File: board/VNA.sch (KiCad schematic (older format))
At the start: 63 parts, among them J1 Conn_01x08, J10 Conn_01x01, J11 Conn_01x01, J12 Conn_01x01, J13 Conn_01x01, J14 Conn_01x01, J15 Conn_02x05_Odd_Even, J16 Conn_02x05_Odd_Even, J17 Conn_01x04, J18 Conn_01x01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

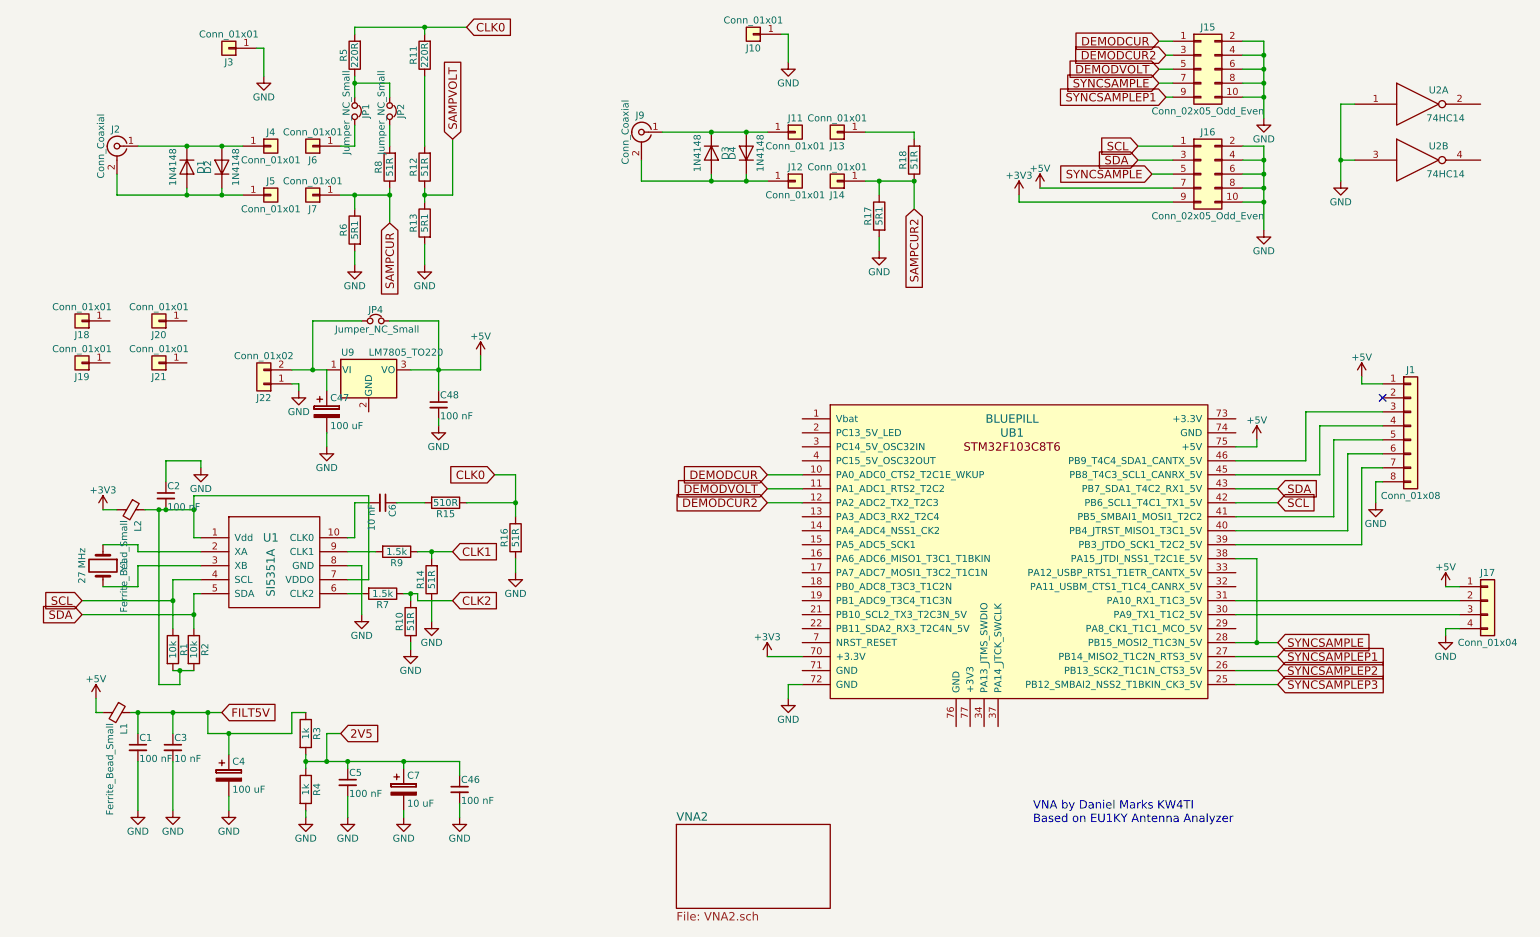
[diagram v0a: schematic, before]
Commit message: Removed useless parts of the board and make some corrections
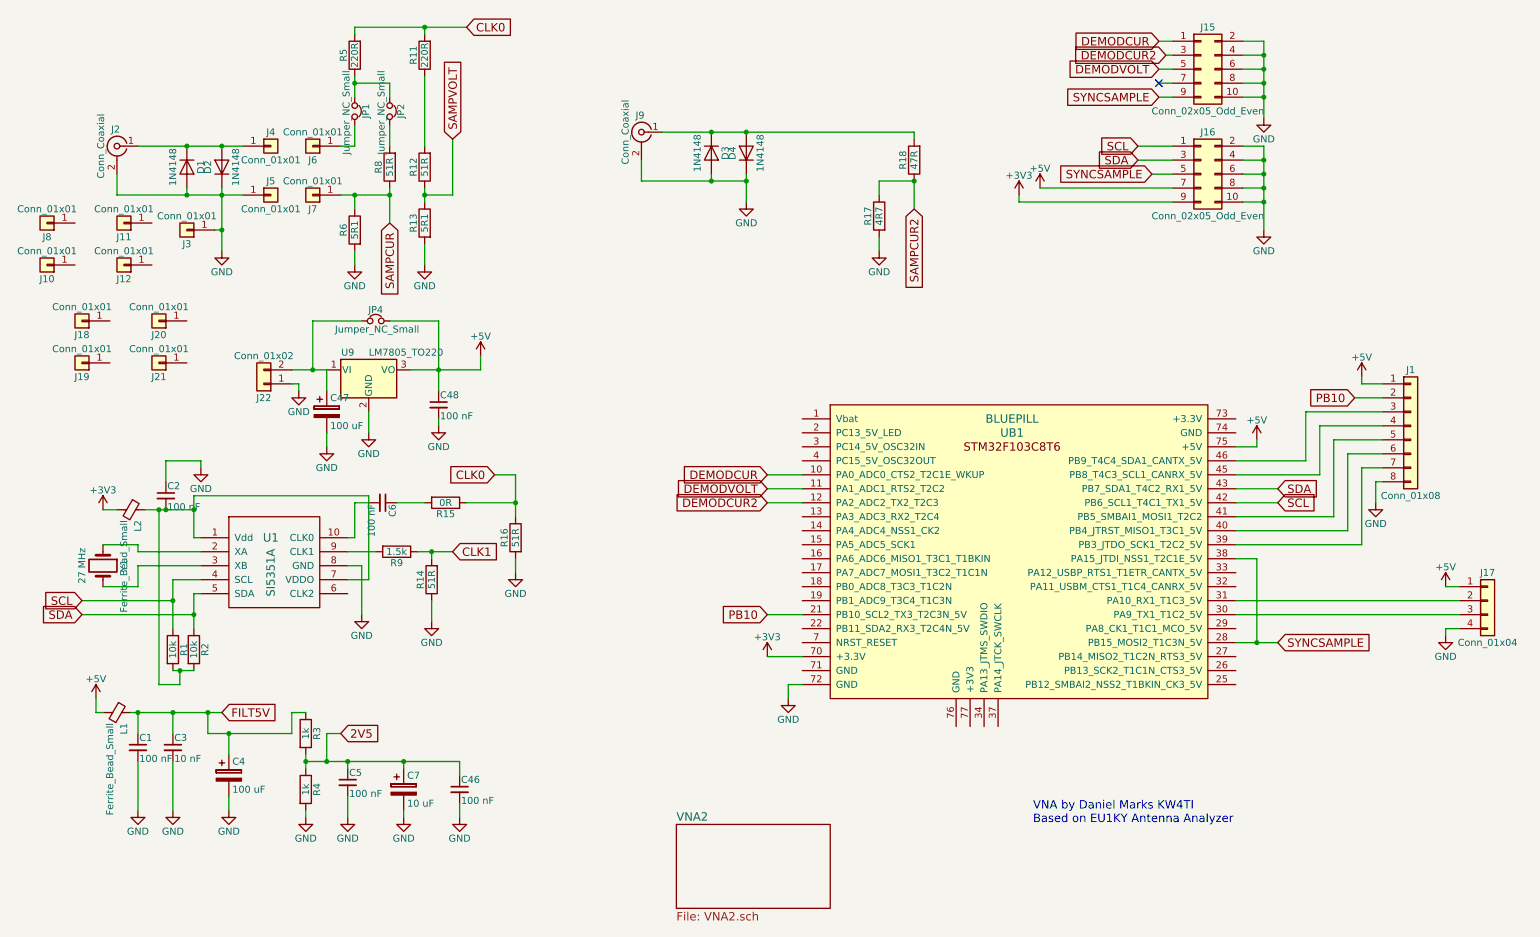
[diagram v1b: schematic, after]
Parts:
- removed J13, J14: Conn_01x01, Connectors:1pin, symbol Conn_01x01
- removed R10: 51R, Resistors_THT:R_Axial_DIN0207_L6.3mm_D2.5mm_P7.62mm_Horizontal, symbol R
- removed R7: 1.5k, Resistors_THT:R_Axial_DIN0207_L6.3mm_D2.5mm_P7.62mm_Horizontal, symbol R
- removed U2: 74HC14, Housings_DIP:DIP-14_W7.62mm_Socket, symbol 74HC14
- added J8: Conn_01x01, Connectors:1pin, symbol Conn_01x01
- C6: value 10 nF -> 100 nF
- R15: value 510R -> 0R
- R17: value 5R1 -> 4R7
- R18: value 51R -> 47R
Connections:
- net GND: now also D1.2 (A), D2.1 (K), D3.2 (A), D4.1 (K), J2.2 (Ext), J5.1 (Pin_1), J9.2 (Ext), U9.2 (GND); no longer J10.1 (Pin_1)
- net SYNCSAMPLE: now also J15.9 (Pin_9); no longer J15.7 (Pin_7)
- net PB10: now reaches UB1.21 (PB10_SCL2_TX3_T2C3N_5V)
- net PB10: now also J1.2 (Pin_2)
- net at D3.1 (K), D4.2 (A), J9.1 (In): now also R18.2; no longer J11.1 (Pin_1)
- net SYNCSAMPLEP1: no longer names the net of UB1.27 (PB14_MISO2_T1C2N_RTS3_5V)
- net SYNCSAMPLEP1: no longer J15.9 (Pin_9)
- net SYNCSAMPLEP2: no longer names the net of UB1.26 (PB13_SCK2_T1C1N_CTS3_5V)
- net SYNCSAMPLEP3: no longer names the net of UB1.25 (PB12_SMBAI2_NSS2_T1BKIN_CK3_5V)
- now unconnected: J12.1 (Pin_1)
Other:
- moved on the sheet: J3

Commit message: Added LCD mount
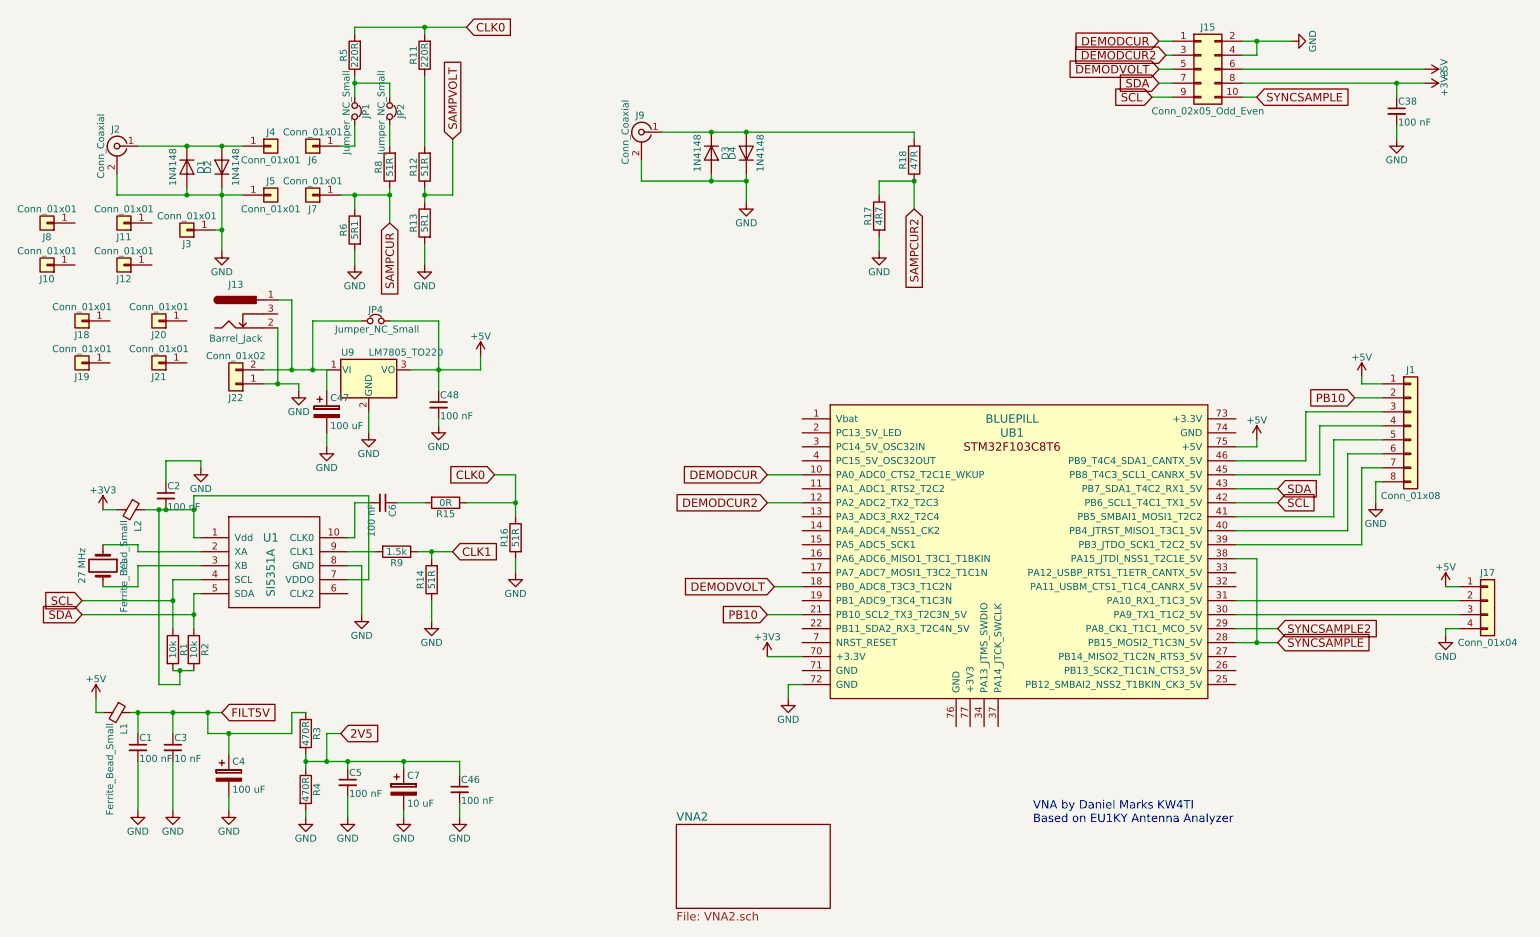
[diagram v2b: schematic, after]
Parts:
- removed J16: Conn_02x05_Odd_Even, Pin_Headers:Pin_Header_Straight_2x05_Pitch2.54mm, symbol Conn_02x05_Odd_Even
- added C38: 100 nF, Capacitors_THT:C_Disc_D5.0mm_W2.5mm_P2.50mm, symbol C_Small
- added J13: Barrel_Jack, Connectors:BARREL_JACK, symbol Barrel_Jack
- R3, R4: value 1k -> 470R
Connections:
- net +3V3: now also J15.8 (Pin_8), C38.1
- net +5V: now also J15.6 (Pin_6)
- net DEMODVOLT: now also UB1.18 (PB0_ADC8_T3C3_T1C2N); no longer UB1.11 (PA1_ADC1_RTS2_T2C2)
- net GND: now also C38.2, J13.2; no longer J15.10 (Pin_10), J15.6 (Pin_6), J15.8 (Pin_8)
- net SCL: now also J15.9 (Pin_9)
- net SDA: now also J15.7 (Pin_7)
- net SYNCSAMPLE: now also J15.10 (Pin_10); no longer J15.9 (Pin_9)
- net SYNCSAMPLE2: now reaches UB1.29 (PA8_CK1_T1C1_MCO_5V)
- net at C47.1, J22.2 (Pin_2), JP4.1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: now also J13.1
- no-connect marks 1 -> 0
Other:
- moved on the sheet: J22

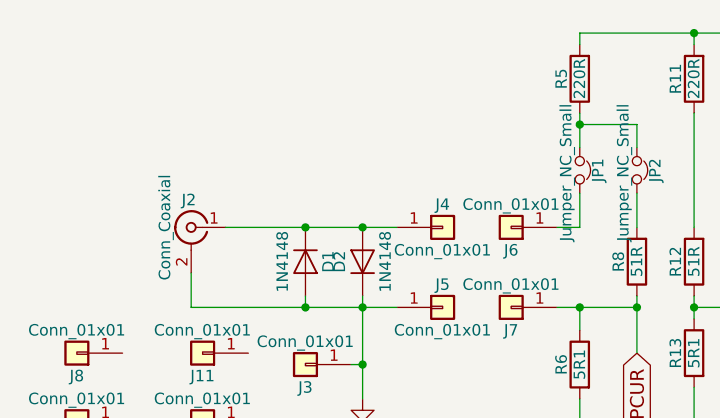
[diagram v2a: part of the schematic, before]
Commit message: Substitute LM339 for 74HC14
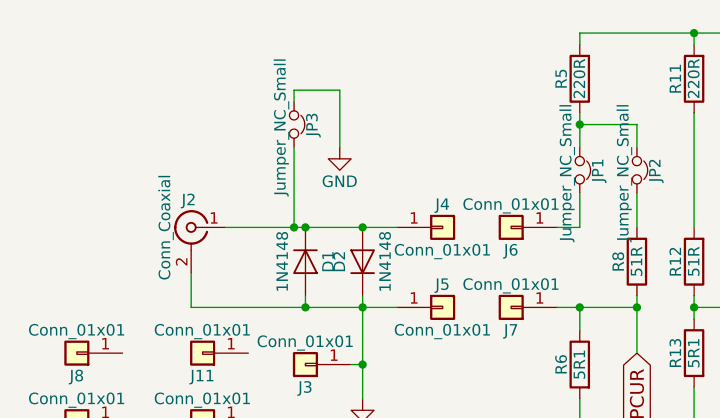
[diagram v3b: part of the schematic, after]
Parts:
- added JP3: Jumper_NC_Small, Pin_Headers:Pin_Header_Straight_1x02_Pitch2.54mm, symbol Jumper_NC_Small
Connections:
- net GND: now also JP3.1
- net at D1.1 (K), D2.2 (A), J2.1 (In)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: now also JP3.2
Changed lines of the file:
@@
 $EndComp
 $Comp
-L +3V3 #PWR23
+L +3V3 #PWR24
 U 1 1 5BB1752D
 P 5850 5700
-F 0 "#PWR23" H 5850 5550 50  0001 C CNN
+F 0 "#PWR24" H 5850 5550 50  0001 C CNN
 F 1 "+3V3" H 5850 5840 50  0000 C CNN
 F 2 "" H 5850 5700 50  0001 C CNN
@@
 $EndComp
 $Comp
-L GND #PWR9
+L GND #PWR10
 U 1 1 5BB1818A
 P 2550 6850
-F 0 "#PWR9" H 2550 6600 50  0001 C CNN
+F 0 "#PWR10" H 2550 6600 50  0001 C CNN
 F 1 "GND" H 2550 6700 50  0000 C CNN
 F 2 "" H 2550 6850 50  0001 C CNN
@@
 $EndComp
 $Comp
-L GND #PWR11
+L GND #PWR12
 U 1 1 5BB182B4
 P 2850 6850
-F 0 "#PWR11" H 2850 6600 50  0001 C CNN
+F 0 "#PWR12" H 2850 6600 50  0001 C CNN
 F 1 "GND" H 2850 6700 50  0000 C CNN
 F 2 "" H 2850 6850 50  0001 C CNN
@@
 $EndComp
 $Comp
-L GND #PWR7
+L GND #PWR8
 U 1 1 5BB18510
 P 2000 6800
-F 0 "#PWR7" H 2000 6550 50  0001 C CNN
+F 0 "#PWR8" H 2000 6550 50  0001 C CNN
 F 1 "GND" H 2000 6650 50  0000 C CNN
 F 2 "" H 2000 6800 50  0001 C CNN
@@
 $EndComp
 $Comp
-L GND #PWR17
+L GND #PWR18
 U 1 1 5BB18D71
 P 3450 5450
-F 0 "#PWR17" H 3450 5200 50  0001 C CNN
+F 0 "#PWR18" H 3450 5200 50  0001 C CNN
 F 1 "GND" H 3450 5300 50  0000 C CNN
 F 2 "" H 3450 5450 50  0001 C CNN
@@
 $EndComp
 $Comp
-L GND #PWR15
+L GND #PWR16
 U 1 1 5BB1B358
 P 3250 6850
-F 0 "#PWR15" H 3250 6600 50  0001 C CNN
+F 0 "#PWR16" H 3250 6600 50  0001 C CNN
 F 1 "GND" H 3250 6700 50  0000 C CNN
 F 2 "" H 3250 6850 50  0001 C CNN
@@
 $EndComp
 $Comp
-L GND #PWR21
+L GND #PWR22
 U 1 1 5BB1D19B
 P 4050 5100
-F 0 "#PWR21" H 4050 4850 50  0001 C CNN
+F 0 "#PWR22" H 4050 4850 50  0001 C CNN
 F 1 "GND" H 4050 4950 50  0000 C CNN
 F 2 "" H 4050 5100 50  0001 C CNN
@@
 $EndComp
 $Comp
-L GND #PWR12
+L GND #PWR13
 U 1 1 5BB20C8C
 P 2900 2900
-F 0 "#PWR12" H 2900 2650 50  0001 C CNN
+F 0 "#PWR13" H 2900 2650 50  0001 C CNN
 F 1 "GND" H 2900 2750 50  0000 C CNN
 F 2 "" H 2900 2900 50  0001 C CNN
@@
 $EndComp
 $Comp
-L GND #PWR16
+L GND #PWR17
 U 1 1 5BB222C0
 P 3400 2900
-F 0 "#PWR16" H 3400 2650 50  0001 C CNN
+F 0 "#PWR17" H 3400 2650 50  0001 C CNN
 F 1 "GND" H 3400 2750 50  0000 C CNN
 F 2 "" H 3400 2900 50  0001 C CNN
@@
 SYNCSAMPLE
 $Comp
-L +5V #PWR26
+L +5V #PWR27
 U 1 1 5BB2CE22
 P 9350 4150
-F 0 "#PWR26" H 9350 4000 50  0001 C CNN
+F 0 "#PWR27" H 9350 4000 50  0001 C CNN
 F 1 "+5V" H 9350 4290 50  0000 C CNN
 F 2 "" H 9350 4150 50  0001 C CNN
@@
 $EndComp
 $Comp
-L GND #PWR24
+L GND #PWR25
 U 1 1 5BB2D2D6
 P 6000 6000
-F 0 "#PWR24" H 6000 5750 50  0001 C CNN
+F 0 "#PWR25" H 6000 5750 50  0001 C CNN
 F 1 "GND" H 6000 5850 50  0000 C CNN
 F 2 "" H 6000 6000 50  0001 C CNN
@@
 $EndComp
 $Comp
-L GND #PWR25
+L GND #PWR26
 U 1 1 5BB350C1
 P 6650 2800
-F 0 "#PWR25" H 6650 2550 50  0001 C CNN
+F 0 "#PWR26" H 6650 2550 50  0001 C CNN
 F 1 "GND" H 6650 2650 50  0000 C CNN
 F 2 "" H 6650 2800 50  0001 C CNN
@@
 DEMODCUR2
 $Comp
-L GND #PWR13
+L GND #PWR14
 U 1 1 5BB4A165
 P 2950 5400
-F 0 "#PWR13" H 2950 5150 50  0001 C CNN
+F 0 "#PWR14" H 2950 5150 50  0001 C CNN
 F 1 "GND" H 2950 5250 50  0000 C CNN
 F 2 "" H 2950 5400 50  0001 C CNN
@@
 SDA
 $Comp
-L +5V #PWR31
+L +5V #PWR32
 U 1 1 5BB21FDF
 P 10550 1500
-F 0 "#PWR31" H 10550 1350 50  0001 C CNN
+F 0 "#PWR32" H 10550 1350 50  0001 C CNN
 F 1 "+5V" H 10550 1640 50  0000 C CNN
 F 2 "" H 10550 1500 50  0001 C CNN
@@
 $EndComp
 $Comp
-L GND #PWR27
+L GND #PWR28
 U 1 1 5BB38EDB
 P 9600 1300
-F 0 "#PWR27" H 9600 1050 50  0001 C CNN
+F 0 "#PWR28" H 9600 1050 50  0001 C CNN
 F 1 "GND" H 9600 1150 50  0000 C CNN
 F 2 "" H 9600 1300 50  0001 C CNN
@@
 $EndComp
 $Comp
-L +5V #PWR33
+L +5V #PWR34
 U 1 1 5BB3F764
 P 10700 5200
-F 0 "#PWR33" H 10700 5050 50  0001 C CNN
+F 0 "#PWR34" H 10700 5050 50  0001 C CNN
 F 1 "+5V" H 10700 5340 50  0000 C CNN
 F 2 "" H 10700 5200 50  0001 C CNN
@@
 $EndComp
 $Comp
-L GND #PWR34
+L GND #PWR35
 U 1 1 5BB3F96D
 P 10700 5550
-F 0 "#PWR34" H 10700 5300 50  0001 C CNN
+F 0 "#PWR35" H 10700 5300 50  0001 C CNN
 F 1 "GND" H 10700 5400 50  0000 C CNN
 F 2 "" H 10700 5550 50  0001 C CNN
@@
 $EndComp
 $Comp
-L GND #PWR8
+L GND #PWR9
 U 1 1 5BB34A68
 P 2500 3800
-F 0 "#PWR8" H 2500 3550 50  0001 C CNN
+F 0 "#PWR9" H 2500 3550 50  0001 C CNN
 F 1 "GND" H 2500 3650 50  0000 C CNN
 F 2 "" H 2500 3800 50  0001 C CNN
@@
 $EndComp
 $Comp
-L +5V #PWR20
+L +5V #PWR21
 U 1 1 5BB34D5D
 P 3800 3550
-F 0 "#PWR20" H 3800 3400 50  0001 C CNN
+F 0 "#PWR21" H 3800 3400 50  0001 C CNN
 F 1 "+5V" H 3800 3690 50  0000 C CNN
 F 2 "" H 3800 3550 50  0001 C CNN
@@
 $EndComp
 $Comp
-L GND #PWR19
+L GND #PWR20
 U 1 1 5BB368A3
 P 3650 6850
-F 0 "#PWR19" H 3650 6600 50  0001 C CNN
+F 0 "#PWR20" H 3650 6600 50  0001 C CNN
 F 1 "GND" H 3650 6700 50  0000 C CNN
 F 2 "" H 3650 6850 50  0001 C CNN
@@
 $EndComp
 $Comp
-L GND #PWR29
+L GND #PWR30
 U 1 1 5BB37FFB
 P 10200 4600
-F 0 "#PWR29" H 10200 4350 50  0001 C CNN
+F 0 "#PWR30" H 10200 4350 50  0001 C CNN
 F 1 "GND" H 10200 4450 50  0000 C CNN
 F 2 "" H 10200 4600 50  0001 C CNN
@@
 $EndComp
 $Comp
-L +5V #PWR28
+L +5V #PWR29
 U 1 1 5BB381D0
 P 10100 3700
-F 0 "#PWR28" H 10100 3550 50  0001 C CNN
+F 0 "#PWR29" H 10100 3550 50  0001 C CNN
 F 1 "+5V" H 10100 3840 50  0000 C CNN
 F 2 "" H 10100 3700 50  0001 C CNN
@@
 $EndComp
 $Comp
-L GND #PWR10
+L GND #PWR11
 U 1 1 5BB39581
 P 2700 4200
-F 0 "#PWR10" H 2700 3950 50  0001 C CNN
+F 0 "#PWR11" H 2700 3950 50  0001 C CNN
 F 1 "GND" H 2700 4050 50  0000 C CNN
 F 2 "" H 2700 4200 50  0001 C CNN
@@
 $EndComp
 $Comp
-L GND #PWR18
+L GND #PWR19
 U 1 1 5BB39BBE
 P 3500 4050
-F 0 "#PWR18" H 3500 3800 50  0001 C CNN
+F 0 "#PWR19" H 3500 3800 50  0001 C CNN
 F 1 "GND" H 3500 3900 50  0000 C CNN
 F 2 "" H 3500 4050 50  0001 C CNN
@@
 $EndComp
 $Comp
-L GND #PWR14
+L GND #PWR15
 U 1 1 5BD7CAFC
 P 3000 4100
-F 0 "#PWR14" H 3000 3850 50  0001 C CNN
+F 0 "#PWR15" H 3000 3850 50  0001 C CNN
 F 1 "GND" H 3000 3950 50  0000 C CNN
 F 2 "" H 3000 4100 50  0001 C CNN
@@
 $EndComp
 $Comp
-L GND #PWR6
+L GND #PWR7
 U 1 1 5BE152F4
 P 1950 2800
-F 0 "#PWR6" H 1950 2550 50  0001 C CNN
+F 0 "#PWR7" H 1950 2550 50  0001 C CNN
 F 1 "GND" H 1950 2650 50  0000 C CNN
 F 2 "" H 1950 2800 50  0001 C CNN
@@
 $EndComp
 $Comp
-L GND #PWR22
+L GND #PWR23
 U 1 1 5BE16D13
 P 5700 2450
-F 0 "#PWR22" H 5700 2200 50  0001 C CNN
+F 0 "#PWR23" H 5700 2200 50  0001 C CNN
 F 1 "GND" H 5700 2300 50  0000 C CNN
 F 2 "" H 5700 2450 50  0001 C CNN
@@
 PB10
 $Comp
-L +3V3 #PWR32
+L +3V3 #PWR33
 U 1 1 5BB22189
 P 10550 1600
-F 0 "#PWR32" H 10550 1450 50  0001 C CNN
+F 0 "#PWR33" H 10550 1450 50  0001 C CNN
 F 1 "+3V3" H 10550 1740 50  0000 C CNN
 F 2 "" H 10550 1600 50  0001 C CNN
@@
 $EndComp
 $Comp
-L GND #PWR30
+L GND #PWR31
 U 1 1 5BE3A08F
 P 10350 2000
-F 0 "#PWR30" H 10350 1750 50  0001 C CNN
+F 0 "#PWR31" H 10350 1750 50  0001 C CNN
 F 1 "GND" H 10350 1850 50  0000 C CNN
 F 2 "" H 10350 2000 50  0001 C CNN
@@
 Wire Wire Line
 	5900 5200 6100 5200
+$Comp
+L Jumper_NC_Small JP3
+U 1 1 5BF04F62
+P 1650 1600
+F 0 "JP3" H 1650 1680 50  0000 C CNN
+F 1 "Jumper_NC_Small" H 1660 1540 50  0000 C CNN
+F 2 "Pin_Headers:Pin_Header_Straight_1x02_Pitch2.54mm" H 1650 1600 50  0001 C CNN
+F 3 "" H 1650 1600 50  0001 C CNN
+	1    1650 1600
+	0    1    1    0
+$EndComp
+$Comp
+L GND #PWR6
+U 1 1 5BF05042
+P 1850 1700
+F 0 "#PWR6" H 1850 1450 50  0001 C CNN
+F 1 "GND" H 1850 1550 50  0000 C CNN
+F 2 "" H 1850 1700 50  0001 C CNN
+F 3 "" H 1850 1700 50  0001 C CNN
+	1    1850 1700
+	1    0    0    -1
+$EndComp
+Wire Wire Line
+	1650 1700 1650 2050
+Connection ~ 1650 2050
+Wire Wire Line
+	1650 1500 1650 1450
+Wire Wire Line
+	1650 1450 1850 1450
+Wire Wire Line
+	1850 1450 1850 1700
 $EndSCHEMATC

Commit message: JLCPCB order 2018-12-01
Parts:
- removed JP1, JP2: Jumper_NC_Small, Pin_Headers:Pin_Header_Straight_1x02_Pitch2.54mm, symbol Jumper_NC_Small
- added C39, C40: 100 nF, Capacitors_THT:C_Disc_D5.0mm_W2.5mm_P2.50mm, symbol C_Small
- added JP1: Jumper_NC_Dual, Pin_Headers:Pin_Header_Straight_1x03_Pitch2.54mm, symbol Jumper_NC_Dual
- added Q1: 2N3904, TO_SOT_Packages_THT:TO-92_Molded_Narrow, symbol 2N3904
- added R38, R39: 1k, Resistors_THT:R_Axial_DIN0207_L6.3mm_D2.5mm_P7.62mm_Horizontal, symbol R
- added R40: 51R, Resistors_THT:R_Axial_DIN0207_L6.3mm_D2.5mm_P7.62mm_Horizontal, symbol R
- R15: value 0R -> 51R
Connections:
- net +3V3: now also J15.6 (Pin_6); no longer J15.8 (Pin_8)
- net +5V: now also J15.4 (Pin_4); no longer J15.6 (Pin_6)
- net 2V5: now also C40.1
- net CLK0: now also C6.2; no longer R15.1, R16.1
- net DEMODCUR: now also J15.3 (Pin_3); no longer J15.1 (Pin_1)
- net DEMODCUR2: now also J15.1 (Pin_1); no longer J15.3 (Pin_3)
- net GND: now also C39.2, C40.2, Q1.1 (E), R40.1; no longer J15.4 (Pin_4), R16.2
- net ATTEN: now reaches UB1.27 (PB14_MISO2_T1C2N_RTS3_5V)
- net ATTEN: now also J15.8 (Pin_8), R39.2
- net at U1.10 (CLK0): now also R15.2; no longer C6.2
- net at C6.1: now also R15.1, R16.1, R40.2; no longer R15.2
- net at J6.1 (Pin_1): now also JP1.3
- net at R8.2: now also JP1.1
- net at R5.1: now also JP1.2
- new net: Q1.3 (C), R16.2
- new net: Q1.2 (B), R38.1
- new net: C39.1, R38.2, R39.1
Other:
- moved on the sheet: C6, R5
